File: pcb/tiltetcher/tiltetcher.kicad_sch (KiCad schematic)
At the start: 10 parts, among them J1 Peltier_Terminal, J2 12V_Terminal, J3 Sensor_Terminal, K1 ADW11, Q1 IRF3205

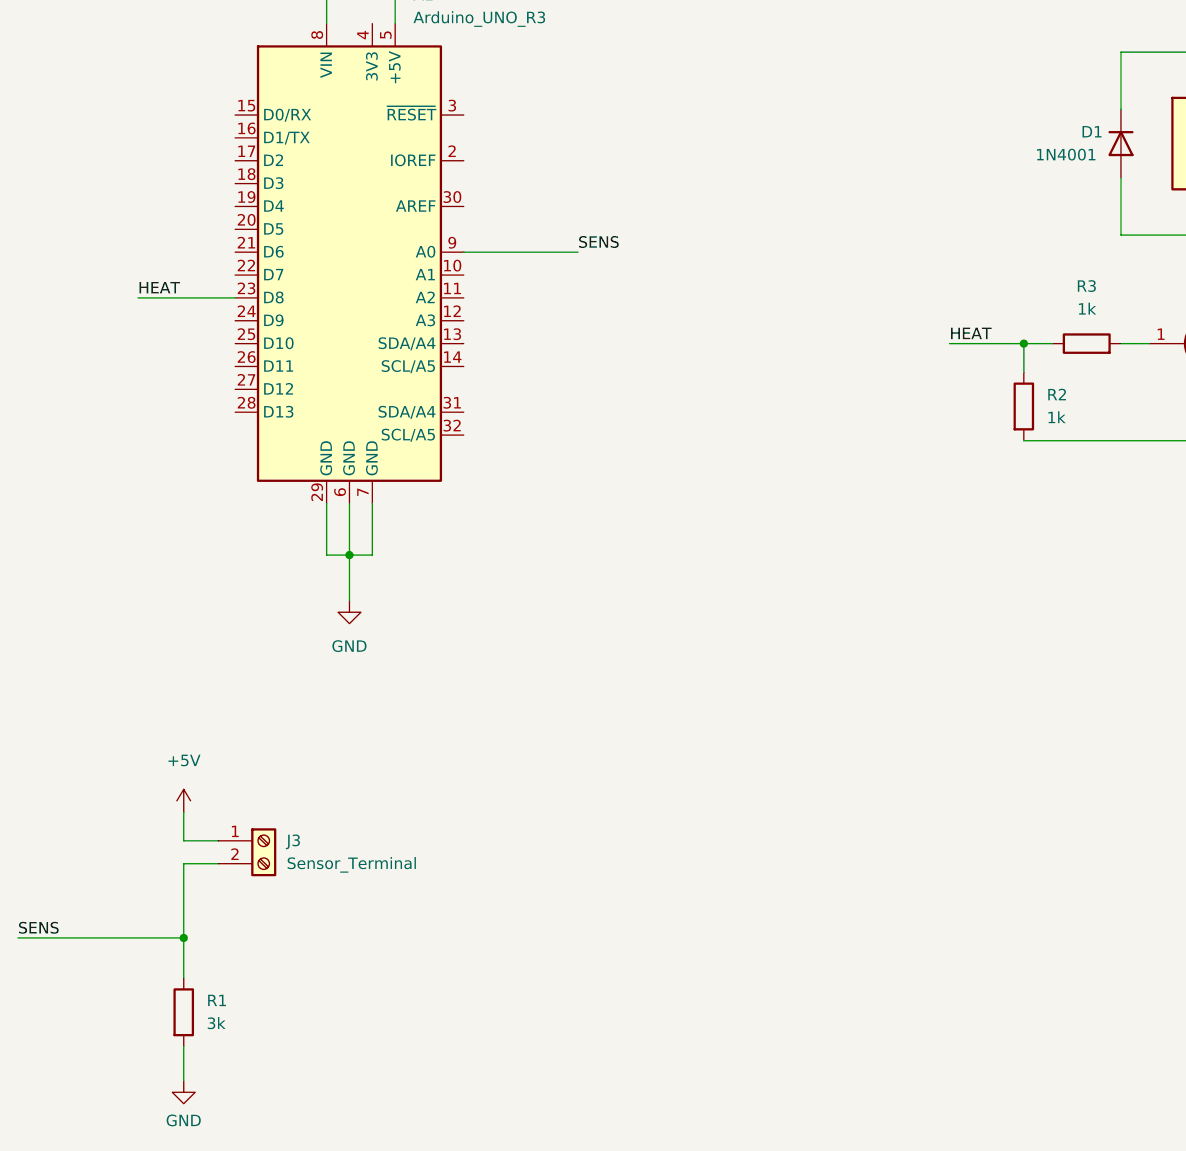
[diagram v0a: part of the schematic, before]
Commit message: added heater LED
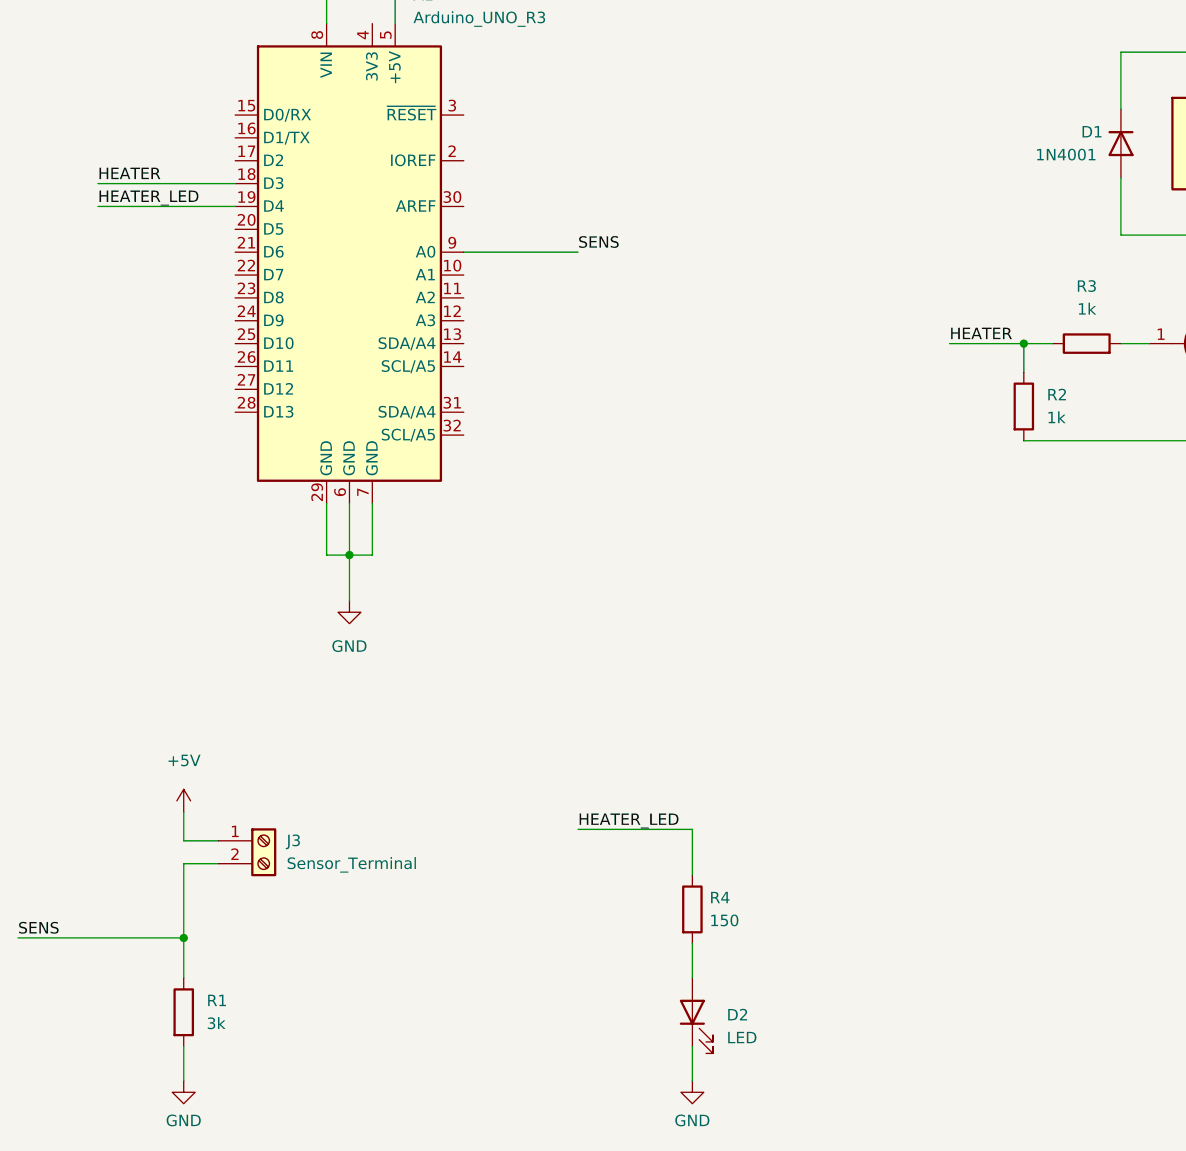
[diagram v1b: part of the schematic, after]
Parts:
- added D2: LED, symbol Device:LED
- added R4: 150, Resistor_THT:R_Axial_DIN0207_L6.3mm_D2.5mm_P10.16mm_Horizontal, symbol Device:R
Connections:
- net GND: now also D2.1 (K)
- net HEATER: now reaches A1.18 (D3)
- net HEATER: now also R2.1, R3.1
- net HEATER_LED: now reaches A1.19 (D4)
- net HEATER_LED: now also R4.1
- removed net HEAT: A1.23 (D8), R2.1, R3.1
- new net: D2.2 (A), R4.2
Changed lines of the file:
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@@
+    (stroke (width 0) (type default) (color 0 0 0 0))
+  )
+  (wire (pts (xy 36.195 80.645) (xy 51.435 80.645))
     (stroke (width 0) (type default) (color 0 0 0 0))
   )
@@
     (stroke (width 0) (type default) (color 0 0 0 0))
   )
+  (wire (pts (xy 102.235 149.86) (xy 102.235 154.94))
+    (stroke (width 0) (type default) (color 0 0 0 0))
+  )
   (wire (pts (xy 173.355 60.96) (xy 180.34 60.96))
     (stroke (width 0) (type default) (color 0 0 0 0))
@@
     (stroke (width 0) (type default) (color 0 0 0 0))
   )
-  (wire (pts (xy 40.64 90.805) (xy 51.435 90.805))
+  (wire (pts (xy 89.535 149.86) (xy 102.235 149.86))
+    (stroke (width 0) (type default) (color 0 0 0 0))
+  )
+  (wire (pts (xy 36.195 78.105) (xy 51.435 78.105))
+    (stroke (width 0) (type default) (color 0 0 0 0))
+  )
+  (wire (pts (xy 102.235 162.56) (xy 102.235 166.37))
     (stroke (width 0) (type default) (color 0 0 0 0))
   )
   (wire (pts (xy 61.595 119.38) (xy 64.135 119.38))
+    (stroke (width 0) (type default) (color 0 0 0 0))
+  )
+  (wire (pts (xy 102.235 173.99) (xy 102.235 177.8))
     (stroke (width 0) (type default) (color 0 0 0 0))
   )
@@
     (effects (font (size 1.27 1.27)) (justify left bottom))
   )
-  (label "HEAT" (at 40.64 90.805 0)
+  (label "HEATER_LED" (at 89.535 149.86 0)
+    (effects (font (size 1.27 1.27)) (justify left bottom))
+  )
+  (label "HEATER_LED" (at 36.195 80.645 0)
+    (effects (font (size 1.27 1.27)) (justify left bottom))
+  )
+  (label "HEATER" (at 36.195 78.105 0)
     (effects (font (size 1.27 1.27)) (justify left bottom))
   )
@@
     (effects (font (size 1.27 1.27)) (justify left bottom))
   )
-  (label "HEAT" (at 130.81 95.885 0)
+  (label "HEATER" (at 130.81 95.885 0)
     (effects (font (size 1.27 1.27)) (justify left bottom))
   )
@@
     (pin "1")
   )
+  (symbol (lib_id "power:GND") (at 102.235 177.8 0) (unit 1)
+    (in_bom yes) (on_board yes) (fields_autoplaced)
+    (property "Reference" "#PWR07" (id 0) (at 102.235 184.15 0)
+      (effects (font (size 1.27 1.27)) hide)
+    )
+    (property "Value" "GND" (id 1) (at 102.235 182.245 0))
+    (property "Footprint" "" (id 2) (at 102.235 177.8 0)
+      (effects (font (size 1.27 1.27)) hide)
+    )
+    (property "Datasheet" "" (id 3) (at 102.235 177.8 0)
+      (effects (font (size 1.27 1.27)) hide)
+    )
+    (pin "1")
+  )
   (symbol (lib_id "power:GND") (at 64.135 124.46 0) (unit 1)
     (in_bom yes) (on_board yes) (fields_autoplaced)
@@
     )
     (pin "1")
+  )
+  (symbol (lib_id "Device:R") (at 102.235 158.75 0) (unit 1)
+    (in_bom yes) (on_board yes) (fields_autoplaced)
+    (property "Reference" "R4" (id 0) (at 104.14 157.4799 0)
+      (effects (font (size 1.27 1.27)) (justify left))
+    )
+    (property "Value" "150" (id 1) (at 104.14 160.0199 0)
+      (effects (font (size 1.27 1.27)) (justify left))
+    )
+    (property "Footprint" "Resistor_THT:R_Axial_DIN0207_L6.3mm_D2.5mm_P10.16mm_Horizontal" (id 2) (at 100.457 158.75 90)
+      (effects (font (size 1.27 1.27)) hide)
+    )
+    (property "Datasheet" "~" (id 3) (at 102.235 158.75 0)
+      (effects (font (size 1.27 1.27)) hide)
+    )
+    (pin "1")
+    (pin "2")
   )
   (symbol (lib_id "Device:R") (at 146.05 95.885 90) (unit 1)
@@
     )
     (property "Datasheet" "~" (id 3) (at 146.05 95.885 0)
+      (effects (font (size 1.27 1.27)) hide)
+    )
+    (pin "1")
+    (pin "2")
+  )
+  (symbol (lib_id "Device:LED") (at 102.235 170.18 90) (unit 1)
+    (in_bom yes) (on_board yes) (fields_autoplaced)
+    (property "Reference" "D2" (id 0) (at 106.045 170.4974 90)
+      (effects (font (size 1.27 1.27)) (justify right))
+    )
+    (property "Value" "LED" (id 1) (at 106.045 173.0374 90)
+      (effects (font (size 1.27 1.27)) (justify right))
+    )
+    (property "Footprint" "" (id 2) (at 102.235 170.18 0)
+      (effects (font (size 1.27 1.27)) hide)
+    )
+    (property "Datasheet" "~" (id 3) (at 102.235 170.18 0)
       (effects (font (size 1.27 1.27)) hide)
     )
@@
       (reference "#PWR06") (unit 1) (value "+12V") (footprint "")
     )
+    (path "/07adceca-6d92-4f56-bf12-054a81790991"
+      (reference "#PWR07") (unit 1) (value "GND") (footprint "")
+    )
     (path "/9871fda3-eba1-4dcc-b428-e392a4db563a"
       (reference "#PWR0101") (unit 1) (value "GND") (footprint "")
@@
       (reference "D1") (unit 1) (value "1N4001") (footprint "Diode_THT:D_DO-41_SOD81_P10.16mm_Horizontal")
     )
+    (path "/bbe7bc1a-3c29-49d6-8dfe-7cdf16c8cbb6"
+      (reference "D2") (unit 1) (value "LED") (footprint "")
+    )
     (path "/dffd1ab6-898c-41e1-96bf-12be5cd6611d"
       (reference "J1") (unit 1) (value "Peltier_Terminal") (footprint "TerminalBlock:TerminalBlock_bornier-2_P5.08mm")
@@
       (reference "R3") (unit 1) (value "1k") (footprint "Resistor_THT:R_Axial_DIN0207_L6.3mm_D2.5mm_P10.16mm_Horizontal")
     )
-  )
+    (path "/a3c6301a-3d8a-484d-914c-2bc6b85237c2"
+      (reference "R4") (unit 1) (value "150") (footprint "Resistor_THT:R_Axial_DIN0207_L6.3mm_D2.5mm_P10.16mm_Horizontal")
+    )
+  )

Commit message: lcd temperature
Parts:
- removed D2: LED, symbol Device:LED
- removed J1: Peltier_Terminal, TerminalBlock:TerminalBlock_bornier-2_P5.08mm, symbol Connector:Screw_Terminal_01x02
- removed J2: 12V_Terminal, TerminalBlock:TerminalBlock_bornier-2_P5.08mm, symbol Connector:Screw_Terminal_01x02
- removed J3: Sensor_Terminal, TerminalBlock:TerminalBlock_bornier-2_P5.08mm, symbol Connector:Screw_Terminal_01x02
- removed R1: 3k, Resistor_THT:R_Axial_DIN0207_L6.3mm_D2.5mm_P10.16mm_Horizontal, symbol Device:R
- removed R4: 150, Resistor_THT:R_Axial_DIN0207_L6.3mm_D2.5mm_P10.16mm_Horizontal, symbol Device:R
- added J?: Jack-DC, symbol Connector:Jack-DC
- added J?: Screw_Terminal_left, symbol Connector:Screw_Terminal_01x11
- added J?: Screw_Terminal_right, symbol Connector:Screw_Terminal_01x11
- added M?: Motor_DC, symbol Motor:Motor_DC
- added R?: Heater, symbol Device:Heater
- added R?: 3k, Resistor_THT:R_Axial_DIN0207_L6.3mm_D2.5mm_P10.16mm_Horizontal, symbol Device:R
- added SW?: SW_DIP_Heater, symbol Switch:SW_DIP_x01
- added SW?: SW_DIP_Motor, symbol Switch:SW_DIP_x01
- added SW?: SW_DIP_Main, symbol Switch:SW_DIP_x01
- added TH?: Thermistor_NTC, symbol Device:Thermistor_NTC
- added U? (x2): LM2596S-Module, symbol Regulator_Switching:LM2596S-Module
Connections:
- net +12V: now also K1.3, SW?.1, SW?.2
- net GND: now also J?.2, J?.6 (Pin_6), J?.6 (Pin_6), R?.2, U?.2 (IN-), U?.2 (IN-); no longer K1.5
- net HEATER: no longer A1.18 (D3)
- net SENS: now also J?.7 (Pin_7), R?.1, TH?.2
- net HEATER_LED: no longer names the net of A1.19 (D4)
- new net: SW?.2, U?.1 (IN+) (x2)
- new net: J?.1, SW?.1
- new net: M?.1 (+), U?.3 (OUT+)
- new net: M?.2 (-), U?.4 (OUT-)
- new net: R?.1, U?.3 (OUT+)
- new net: R?.2, U?.4 (OUT-)
- new net 12V: J?.11 (Pin_11), J?.11 (Pin_11)
- new net 5V: J?.1 (Pin_1)
- new net HEATER+: J?.2 (Pin_2), K1.5, SW?.1
- new net IOREF: J?.3 (Pin_3)
- new net LED_HEATER_NOK+: J?.8 (Pin_8)
- new net LED_HEATER_OK+: J?.9 (Pin_9)
- new net LED_NC+: J?.7 (Pin_7)
- new net LED_POW+: J?.10 (Pin_10)
- new net NC: J?.2 (Pin_2), J?.3 (Pin_3), J?.4 (Pin_4), J?.5 (Pin_5)
- new net RESET: J?.4 (Pin_4)
- new net SCL: J?.10 (Pin_10)
- new net SDA: J?.9 (Pin_9)
- new net SENS_SUPPLY: J?.5 (Pin_5), TH?.1
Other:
- title: (none) -> Tiltetcher V3
- moved on the sheet: A1, D1, K1, Q1, R2, R3
